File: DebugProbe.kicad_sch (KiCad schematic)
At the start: 3 parts, among them J8 Conn_ARM_JTAG_SWD_10, SW1 SW_Push

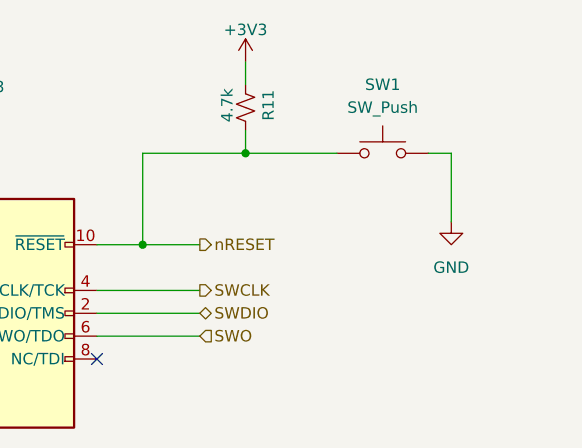
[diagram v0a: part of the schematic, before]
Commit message: replaced soil_sns frontend with SN74
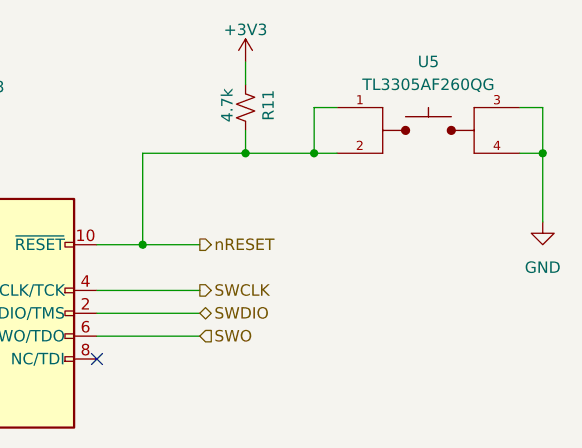
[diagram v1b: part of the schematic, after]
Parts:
- removed SW1: SW_Push, symbol Switch:SW_Push
- added U5: TL3305AF260QG, SproutSenseFootprints:SW_TL3305AF260QG, symbol SproutSense:TL3305AF260QG
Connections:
- net GND: now also U5.3, U5.4
- net nRESET: now also U5.1, U5.2
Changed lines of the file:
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@@
+	)
+	(junction
+		(at 194.31 73.66)
+		(diameter 0)
+		(color 0 0 0 0)
 	)
 	(junction
@@
 		(color 0 0 0 0)
 	)
+	(junction
+		(at 219.71 73.66)
+		(diameter 0)
+		(color 0 0 0 0)
+	)
 	(no_connect
 		(at 154.94 106.68)
@@
 	(wire
 		(pts
+			(xy 217.17 68.58) (xy 219.71 68.58)
+		)
+		(stroke
+			(width 0)
+			(type default)
+		)
+	)
+	(wire
+		(pts
 			(xy 186.69 71.12) (xy 186.69 73.66)
 		)
@@
 	(wire
 		(pts
+			(xy 194.31 73.66) (xy 186.69 73.66)
+		)
+		(stroke
+			(width 0)
+			(type default)
+		)
+	)
+	(wire
+		(pts
+			(xy 194.31 68.58) (xy 194.31 73.66)
+		)
+		(stroke
+			(width 0)
+			(type default)
+		)
+	)
+	(wire
+		(pts
 			(xy 157.48 106.68) (xy 157.48 115.57)
 		)
@@
 	(wire
 		(pts
+			(xy 196.85 68.58) (xy 194.31 68.58)
+		)
+		(stroke
+			(width 0)
+			(type default)
+		)
+	)
+	(wire
+		(pts
 			(xy 170.18 83.82) (xy 175.26 83.82)
 		)
@@
 	(wire
 		(pts
-			(xy 207.01 73.66) (xy 209.55 73.66)
+			(xy 217.17 73.66) (xy 219.71 73.66)
 		)
 		(stroke
@@
 	(wire
 		(pts
-			(xy 209.55 73.66) (xy 209.55 81.28)
+			(xy 219.71 73.66) (xy 219.71 81.28)
 		)
 		(stroke
@@
 	(wire
 		(pts
+			(xy 219.71 68.58) (xy 219.71 73.66)
+		)
+		(stroke
+			(width 0)
+			(type default)
+		)
+	)
+	(wire
+		(pts
 			(xy 175.26 73.66) (xy 175.26 83.82)
 		)
@@
 	(wire
 		(pts
-			(xy 196.85 73.66) (xy 186.69 73.66)
+			(xy 196.85 73.66) (xy 194.31 73.66)
 		)
 		(stroke
@@
 	(symbol
 		(lib_id "power:GND")
-		(at 209.55 81.28 0)
+		(at 219.71 81.28 0)
 		(unit 1)
 		(exclude_from_sim no)
@@
 		(fields_autoplaced yes)
 		(property "Reference" "#PWR054"
-			(at 209.55 87.63 0)
+			(at 219.71 87.63 0)
 			(effects
 				(font
@@
 		)
 		(property "Value" "GND"
-			(at 209.55 86.36 0)
+			(at 219.71 86.36 0)
 			(effects
 				(font
@@
 		)
 		(property "Footprint" ""
-			(at 209.55 81.28 0)
+			(at 219.71 81.28 0)
 			(effects
 				(font
@@
 		)
 		(property "Datasheet" ""
-			(at 209.55 81.28 0)
+			(at 219.71 81.28 0)
 			(effects
 				(font
@@
 		)
 		(property "Description" "Power symbol creates a global label with name \"GND\" , ground"
-			(at 209.55 81.28 0)
+			(at 219.71 81.28 0)
 			(effects
 				(font
@@
 	)
 	(symbol
+		(lib_id "SproutSense:TL3305AF260QG")
+		(at 207.01 71.12 0)
+		(unit 1)
+		(exclude_from_sim no)
+		(in_bom yes)
+		(on_board yes)
+		(dnp no)
+		(fields_autoplaced yes)
+		(property "Reference" "U5"
+			(at 207.01 63.5 0)
+			(effects
+				(font
+					(size 1.27 1.27)
+				)
+			)
+		)
+		(property "Value" "TL3305AF260QG"
+			(at 207.01 66.04 0)
+			(effects
+				(font
+					(size 1.27 1.27)
+				)
+			)
+		)
+		(property "Footprint" "SproutSenseFootprints:SW_TL3305AF260QG"
+			(at 207.01 71.12 0)
+			(effects
+				(font
+					(size 1.27 1.27)
+				)
+				(justify bottom)
+				(hide yes)
+			)
+		)
+		(property "Datasheet" "https://configured-product-images.s3.amazonaws.com/Datasheets/TL3305.pdf"
+			(at 207.01 71.12 0)
+			(effects
+				(font
+					(size 1.27 1.27)
+				)
+				(hide yes)
+			)
+		)
+		(property "Description" "SWITCH TACTILE SPST-NO 0.05A 12V"
+			(at 207.01 71.12 0)
+			(effects
+				(font
+					(size 1.27 1.27)
+				)
+				(hide yes)
+			)
+		)
+		(property "PARTREV" "C"
+			(at 207.01 71.12 0)
+			(effects
+				(font
+					(size 1.27 1.27)
+				)
+				(justify bottom)
+				(hide yes)
+			)
+		)
+		(property "MANUFACTURER" "E-Switch"
+			(at 207.01 71.12 0)
+			(effects
+				(font
+					(size 1.27 1.27)
+				)
+				(justify bottom)
+				(hide yes)
+			)
+		)
+		(property "MAXIMUM_PACKAGE_HEIGHT" "3.8mm"
+			(at 207.01 71.12 0)
+			(effects
+				(font
+					(size 1.27 1.27)
+				)
+				(justify bottom)
+				(hide yes)
+			)
+		)
+		(property "STANDARD" "Manufacturer recommendations"
+			(at 207.01 71.12 0)
+			(effects
+				(font
+					(size 1.27 1.27)
+				)
+				(justify bottom)
+				(hide yes)
+			)
+		)
+		(property "Distributor Prt #" "EG5353CT-ND"
+			(at 207.01 71.12 0)
+			(effects
+				(font
+					(size 1.27 1.27)
+				)
+				(hide yes)
+			)
+		)
+		(property "Manuf Prt #" "TL3305AF260QG"
+			(at 207.01 71.12 0)
+			(effects
+				(font
+					(size 1.27 1.27)
+				)
+				(hide yes)
+			)
+		)
+		(pin "1"
+		)
+		(pin "2"
+		)
+		(pin "3"
+		)
+		(pin "4"
+		)
+		(instances
+			(project ""
+				(path "/6b347550-6a02-4d2d-97d7-e1cbb1403859/a756c159-ba2f-4b88-9b42-3ae8d7fc2cb0"
+					(reference "U5")
+					(unit 1)
+				)
+			)
+		)
+	)
+	(symbol
 		(lib_id "Device:R_Small_US")
 		(at 186.69 68.58 180)
@@
 					(unit 1)
 				)
-			)
-		)
-	)
-	(symbol
-		(lib_id "Switch:SW_Push")
-		(at 201.93 73.66 0)
-		(unit 1)
-		(exclude_from_sim no)
-		(in_bom yes)
-		(on_board yes)
-		(dnp no)
-		(property "Reference" "SW1"
-			(at 201.93 66.04 0)
-			(effects
-				(font
-					(size 1.27 1.27)
-				)
-			)
-		)
-		(property "Value" "SW_Push"
-			(at 201.93 68.58 0)
-			(effects
-				(font
-					(size 1.27 1.27)
-				)
-			)
-		)
-		(property "Footprint" ""
-			(at 201.93 68.58 0)
-			(effects
-				(font
-					(size 1.27 1.27)
-				)
-				(hide yes)
-			)
-		)
-		(property "Datasheet" "~"
-			(at 201.93 68.58 0)
-			(effects
-				(font
-					(size 1.27 1.27)
-				)
-				(hide yes)
-			)
-		)
-		(property "Description" "Push button switch, generic, two pins"
-			(at 201.93 73.66 0)
-			(effects
-				(font
-					(size 1.27 1.27)
-				)
-				(hide yes)
-			)
-		)
-		(pin "1"
-		)
-		(pin "2"
-		)
-		(instances
-			(project ""
-				(path "/6b347550-6a02-4d2d-97d7-e1cbb1403859/a756c159-ba2f-4b88-9b42-3ae8d7fc2cb0"
-					(reference "SW1")
-					(unit 1)
-				)

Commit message: updated schematic for pwr savings
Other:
- title: SproutSyncProto-A-01 -> SproutSyncProto-A-02

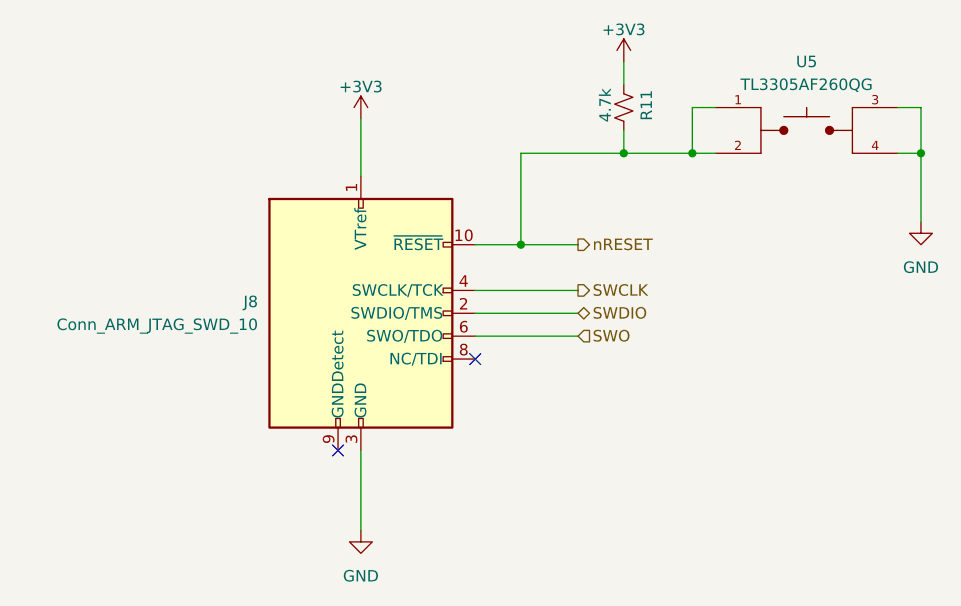
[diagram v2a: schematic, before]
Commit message: updated pcb for pwr savings
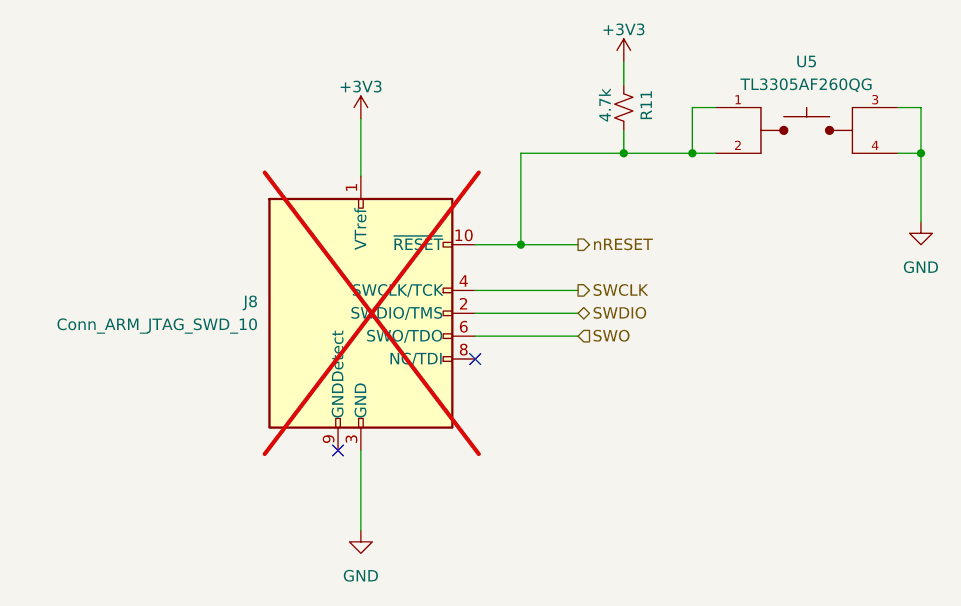
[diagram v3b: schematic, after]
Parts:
- J8: now not fitted
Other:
- title: SproutSyncProto-A-02 -> SproutSyncProto-A-04
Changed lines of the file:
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@@
 	(paper "A4")
 	(title_block
-		(title "SproutSyncProto-A-02")
-		(date "2026-04-29")
+		(title "SproutSyncProto-A-04")
+		(date "2026-05-04")
 		(rev "0.2")
 		(company "SproutSync LTD")
@@
 		(in_bom yes)
 		(on_board yes)
-		(in_pos_files yes)
-		(dnp no)
+		(in_pos_files no)
+		(dnp yes)
 		(fields_autoplaced yes)
 		(property "Reference" "J8"
